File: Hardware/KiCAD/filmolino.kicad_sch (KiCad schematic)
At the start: 37 parts, among them J1 Grove 90°, J2 Grove 90°, J3 Conn_02x15_Odd_Even, J4 AudioJack3, J5 Grove 90°, Q1 BSS138, Q2 BSS138, Q3 BSS138, Q4 BP103B, U1 AQY212GSZ, U2 AQY212GSZ, U3 AQY212SX (550mA), U4 AQY212SX (550mA), U5 SN74LVC1G14DBV

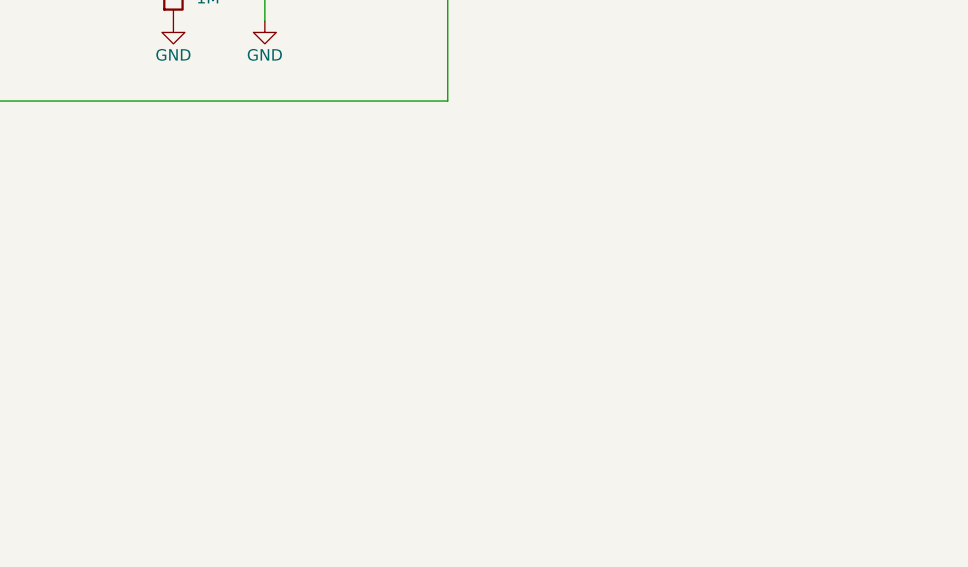
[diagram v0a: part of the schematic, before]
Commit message: Update filmolino.kicad_sch
PCB thichkness and M5Stack module frame added.
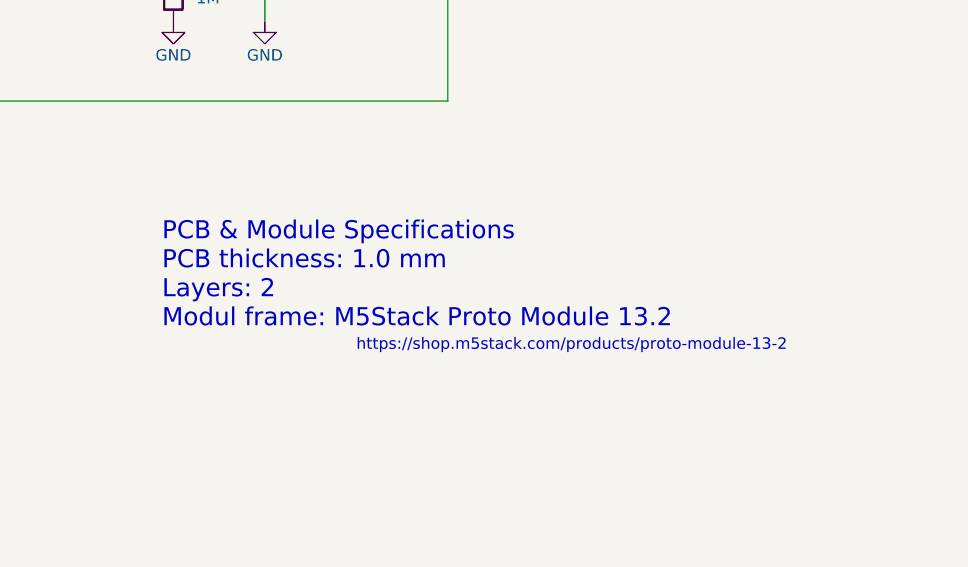
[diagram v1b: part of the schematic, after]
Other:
- note added: "PCB & Module Specifications PCB thickness: 1.0 mm Layers: 2 Modul frame: M5Stack Proto Module 13.2"
- note added: "https://shop.m5stack.com/products/proto-module-13-2"
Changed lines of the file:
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@@
     (effects (font (size 0.8 0.8)) (justify left bottom))
+  )
+  (text "https://shop.m5stack.com/products/proto-module-13-2"
+    (at 198.12 158.75 0)
+    (effects (font (size 1.27 1.27)) (justify left bottom))
   )
   (text "HPWR" (at 101.6 193.04 180)
@@
     (effects (font (size 0.8 0.8)) (justify left bottom))
   )
+  (text "PCB & Module Specifications\nPCB thickness: 1.0 mm\nLayers: 2\nModul frame: M5Stack Proto Module 13.2"
+    (at 176.53 156.21 0)
+    (effects (font (size 2 2)) (justify left bottom))
+  )
   (text "Analog Input\nDigital Output\n+5V Output\nGND" (at 223.52 101.6 0)
